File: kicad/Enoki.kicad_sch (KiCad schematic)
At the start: 14 parts, among them J1 Conn_01x08_Male

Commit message: add jlc fields
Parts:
- C1, C2, C3, C4, C5, C6: JLC (none) -> C377773
- DS1: JLC (none) -> C262569
- R1, R2, R3: JLC (none) -> C25804
- R4: value 390K -> 330K; JLC (none) -> C23137
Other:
- note added: "https://www.buydisplay.com/white-1-3-inch-oled-i2c-arduino-ssd1306-display-module-connector-fpc"
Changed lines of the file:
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@@
     (stroke (width 0) (type default))
   )
+  (text "https://www.buydisplay.com/white-1-3-inch-oled-i2c-arduino-ssd1306-display-module-connector-fpc"
+    (at 63.5 170.18 0)
+    (effects (font (size 1.27 1.27)) (justify left bottom))
+  )
   (text "https://jlcpcb.com/partdetail/Jushuo-AFC07_S30FCA00/C262569"
-    (at 100.33 162.56 0)
-    (effects (font (size 1.27 1.27)) (justify left bottom))
-  )
-  (text "Connector parts:" (at 100.33 160.02 0)
+    (at 63.5 165.1 0)
+    (effects (font (size 1.27 1.27)) (justify left bottom))
+  )
+  (text "Connector parts:" (at 63.5 162.56 0)
     (effects (font (size 1.27 1.27)) (justify left bottom))
   )
@@
       (effects (font (size 1.27 1.27)) hide)
     )
+    (property "JLC" "C25804" (at 119.38 119.38 0)
+      (effects (font (size 1.27 1.27)) hide)
+    )
     (pin "1")
     (pin "2")
@@
       (effects (font (size 1.27 1.27)) hide)
     )
+    (property "JLC" "C377773" (at 140.97 74.93 0)
+      (effects (font (size 1.27 1.27)) hide)
+    )
     (pin "1")
     (pin "2")
@@
       (effects (font (size 1.27 1.27)) hide)
     )
+    (property "JLC" "C25804" (at 119.38 87.63 0)
+      (effects (font (size 1.27 1.27)) hide)
+    )
     (pin "1")
     (pin "2")
@@
       (effects (font (size 1.27 1.27)) hide)
     )
+    (property "JLC" "C377773" (at 137.16 80.01 0)
+      (effects (font (size 1.27 1.27)) hide)
+    )
     (pin "1")
     (pin "2")
@@
       (effects (font (size 1.27 1.27)) hide)
     )
+    (property "JLC" "C377773" (at 140.97 146.05 0)
+      (effects (font (size 1.27 1.27)) hide)
+    )
     (pin "1")
     (pin "2")
@@
       (effects (font (size 1.27 1.27)) hide)
     )
+    (property "JLC" "C377773" (at 154.94 53.34 0)
+      (effects (font (size 1.27 1.27)) hide)
+    )
     (pin "1")
     (pin "2")
@@
     )
     (property "Datasheet" "https://www.vishay.com/docs/37902/oled128o064dbpp3n00000.pdf" (at 157.48 87.63 0)
+      (effects (font (size 1.27 1.27)) hide)
+    )
+    (property "JLC" "C262569" (at 157.48 107.95 0)
       (effects (font (size 1.27 1.27)) hide)
     )
@@
       (effects (font (size 1.27 1.27)))
     )
-    (property "Value" "390K" (at 125.73 147.32 0)
+    (property "Value" "330K" (at 125.73 147.32 0)
       (effects (font (size 1.27 1.27)))
     )
@@
     )
     (property "Datasheet" "~" (at 130.81 146.05 0)
+      (effects (font (size 1.27 1.27)) hide)
+    )
+    (property "JLC" "C23137" (at 130.81 146.05 0)
       (effects (font (size 1.27 1.27)) hide)
     )
@@
       (effects (font (size 1.27 1.27)) hide)
     )
+    (property "JLC" "C25804" (at 119.38 109.22 0)
+      (effects (font (size 1.27 1.27)) hide)
+    )
     (pin "1")
     (pin "2")
@@
       (effects (font (size 1.27 1.27)) hide)
     )
+    (property "JLC" "C377773" (at 160.02 63.5 0)
+      (effects (font (size 1.27 1.27)) hide)
+    )
     (pin "1")
     (pin "2")
@@
       (effects (font (size 1.27 1.27)) hide)
     )
+    (property "JLC" "C377773" (at 157.48 58.42 0)
+      (effects (font (size 1.27 1.27)) hide)
+    )

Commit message: kicad save
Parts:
- DS1: footprint Display:OLED-128O064D -> allen-synthesis:AFC07-S30FCA-00 FPC Connector 30 Pin
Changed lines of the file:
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@@
       (effects (font (size 1.27 1.27)) (justify left))
     )
-    (property "Footprint" "Display:OLED-128O064D" (at 157.48 107.95 0)
+    (property "Footprint" "allen-synthesis:AFC07-S30FCA-00 FPC Connector 30 Pin" (at 157.48 107.95 0)
       (effects (font (size 1.27 1.27)) hide)
     )

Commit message: save
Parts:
- DS1: footprint allen-synthesis:AFC07-S30FCA-00 FPC Connector 30 Pin -> allen-synthesis:KH-FPC0.5-H2.0SMT-30P-QCH FPC Connector 30 pin; JLC C262569 -> C3250002
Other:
- note added: "https://jlcpcb.com/partdetail/3812911-KH_FPC0_5_H2_0SMT_30PQCHF/C3250002"
- note removed: "https://jlcpcb.com/partdetail/Jushuo-AFC07_S30FCA00/C262569"
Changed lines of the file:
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@@
     (effects (font (size 1.27 1.27)) (justify left bottom))
   )
-  (text "https://jlcpcb.com/partdetail/Jushuo-AFC07_S30FCA00/C262569"
+  (text "https://jlcpcb.com/partdetail/3812911-KH_FPC0_5_H2_0SMT_30PQCHF/C3250002"
     (at 63.5 165.1 0)
     (effects (font (size 1.27 1.27)) (justify left bottom))
@@
       (effects (font (size 1.27 1.27)) (justify left))
     )
-    (property "Footprint" "allen-synthesis:AFC07-S30FCA-00 FPC Connector 30 Pin" (at 157.48 107.95 0)
+    (property "Footprint" "allen-synthesis:KH-FPC0.5-H2.0SMT-30P-QCH FPC Connector 30 pin" (at 157.48 107.95 0)
       (effects (font (size 1.27 1.27)) hide)
     )
@@
       (effects (font (size 1.27 1.27)) hide)
     )
-    (property "JLC" "C262569" (at 157.48 107.95 0)
-      (effects (font (size 1.27 1.27)) hide)
-    )
+    (property "JLC" "C3250002" (at 157.48 107.95 0)
+      (effects (font (size 1.27 1.27)) hide)
+    )

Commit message: save
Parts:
- added J2, J3: Conn_01x02_Pin, Connector_PinHeader_2.54mm:PinHeader_1x02_P2.54mm_Vertical_SMD_Pin1Right, symbol Connector:Conn_01x02_Pin
- J1: JLC (none) -> C5160791
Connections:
- no-connect marks 8 -> 12
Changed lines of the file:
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@@
   (no_connect (at 144.78 105.41))
   (no_connect (at 144.78 107.95))
+  (no_connect (at 77.47 127))
+  (no_connect (at 77.47 129.54))
+  (no_connect (at 77.47 114.3))
+  (no_connect (at 77.47 116.84))
   (no_connect (at 77.47 99.06))
   (wire (pts (xy 160.02 59.69) (xy 160.02 49.53))
@@
         (path "/e63e39d7-6ac0-4ffd-8aa3-1841a4541b55"
           (reference "R1") (unit 1)
+        )
+      )
+    )
+  )
+  (symbol (lib_id "Connector:Conn_01x02_Pin") (at 72.39 114.3 0) (unit 1)
+    (in_bom yes) (on_board yes) (dnp no) (fields_autoplaced)
+    (property "Reference" "J2" (at 73.025 109.22 0)
+      (effects (font (size 1.27 1.27)))
+    )
+    (property "Value" "Conn_01x02_Pin" (at 73.025 111.76 0)
+      (effects (font (size 1.27 1.27)))
+    )
+    (property "Footprint" "Connector_PinHeader_2.54mm:PinHeader_1x02_P2.54mm_Vertical_SMD_Pin1Right" (at 72.39 114.3 0)
+      (effects (font (size 1.27 1.27)) hide)
+    )
+    (property "Datasheet" "~" (at 72.39 114.3 0)
+      (effects (font (size 1.27 1.27)) hide)
+    )
+    (property "JLC" "C5160785" (at 72.39 114.3 0)
+      (effects (font (size 1.27 1.27)) hide)
+    )
+    (pin "2")
+    (pin "1")
+    (instances
+      (project "Enoki"
+        (path "/e63e39d7-6ac0-4ffd-8aa3-1841a4541b55"
+          (reference "J2") (unit 1)
         )
       )
@@
       (effects (font (size 1.27 1.27)) hide)
     )
+    (property "JLC" "C5160791" (at 72.39 88.9 0)
+      (effects (font (size 1.27 1.27)) hide)
+    )
     (pin "1")
     (pin "2")
@@
         )
       )
+    )
+  )
+  (symbol (lib_id "Connector:Conn_01x02_Pin") (at 72.39 127 0) (unit 1)
+    (in_bom yes) (on_board yes) (dnp no) (fields_autoplaced)
+    (property "Reference" "J3" (at 73.025 121.92 0)
+      (effects (font (size 1.27 1.27)))
+    )
+    (property "Value" "Conn_01x02_Pin" (at 73.025 124.46 0)
+      (effects (font (size 1.27 1.27)))
+    )
+    (property "Footprint" "Connector_PinHeader_2.54mm:PinHeader_1x02_P2.54mm_Vertical_SMD_Pin1Right" (at 72.39 127 0)
+      (effects (font (size 1.27 1.27)) hide)
+    )
+    (property "Datasheet" "~" (at 72.39 127 0)
+      (effects (font (size 1.27 1.27)) hide)
+    )
+    (property "JLC" "C5160785" (at 72.39 127 0)
+      (effects (font (size 1.27 1.27)) hide)
+    )
+    (pin "2")
+    (pin "1")
+    (instances
+      (project "Enoki"
+        (path "/e63e39d7-6ac0-4ffd-8aa3-1841a4541b55"
+          (reference "J3") (unit 1)
+        )
+      )

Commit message: save
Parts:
- JP1, JP2: footprint Jumper:SolderJumper-2_P1.3mm_Open_RoundedPad1.0x1.5mm -> Jumper:SolderJumper-2_P1.3mm_Bridged_RoundedPad1.0x1.5mm
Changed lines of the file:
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@@
       (effects (font (size 1.27 1.27)) (justify right))
     )
-    (property "Footprint" "Jumper:SolderJumper-2_P1.3mm_Open_RoundedPad1.0x1.5mm" (at 119.38 78.74 0)
+    (property "Footprint" "Jumper:SolderJumper-2_P1.3mm_Bridged_RoundedPad1.0x1.5mm" (at 119.38 78.74 0)
       (effects (font (size 1.27 1.27)) hide)
     )
@@
       (effects (font (size 1.27 1.27)) hide)
     )
-    (pin "2")
-    (pin "1")
+    (pin "1")
+    (pin "2")
     (instances
       (project "Enoki"
@@
       (effects (font (size 1.27 1.27)))
     )
-    (property "Footprint" "Jumper:SolderJumper-2_P1.3mm_Open_RoundedPad1.0x1.5mm" (at 137.16 118.11 0)
+    (property "Footprint" "Jumper:SolderJumper-2_P1.3mm_Bridged_RoundedPad1.0x1.5mm" (at 137.16 118.11 0)
       (effects (font (size 1.27 1.27)) hide)
     )
@@
       (effects (font (size 1.27 1.27)) hide)
     )
-    (pin "2")
-    (pin "1")
-    (instances
-      (project "Enoki"
+    (pin "1")
+    (pin "2")
+    (instances
+      (project "Enoki"

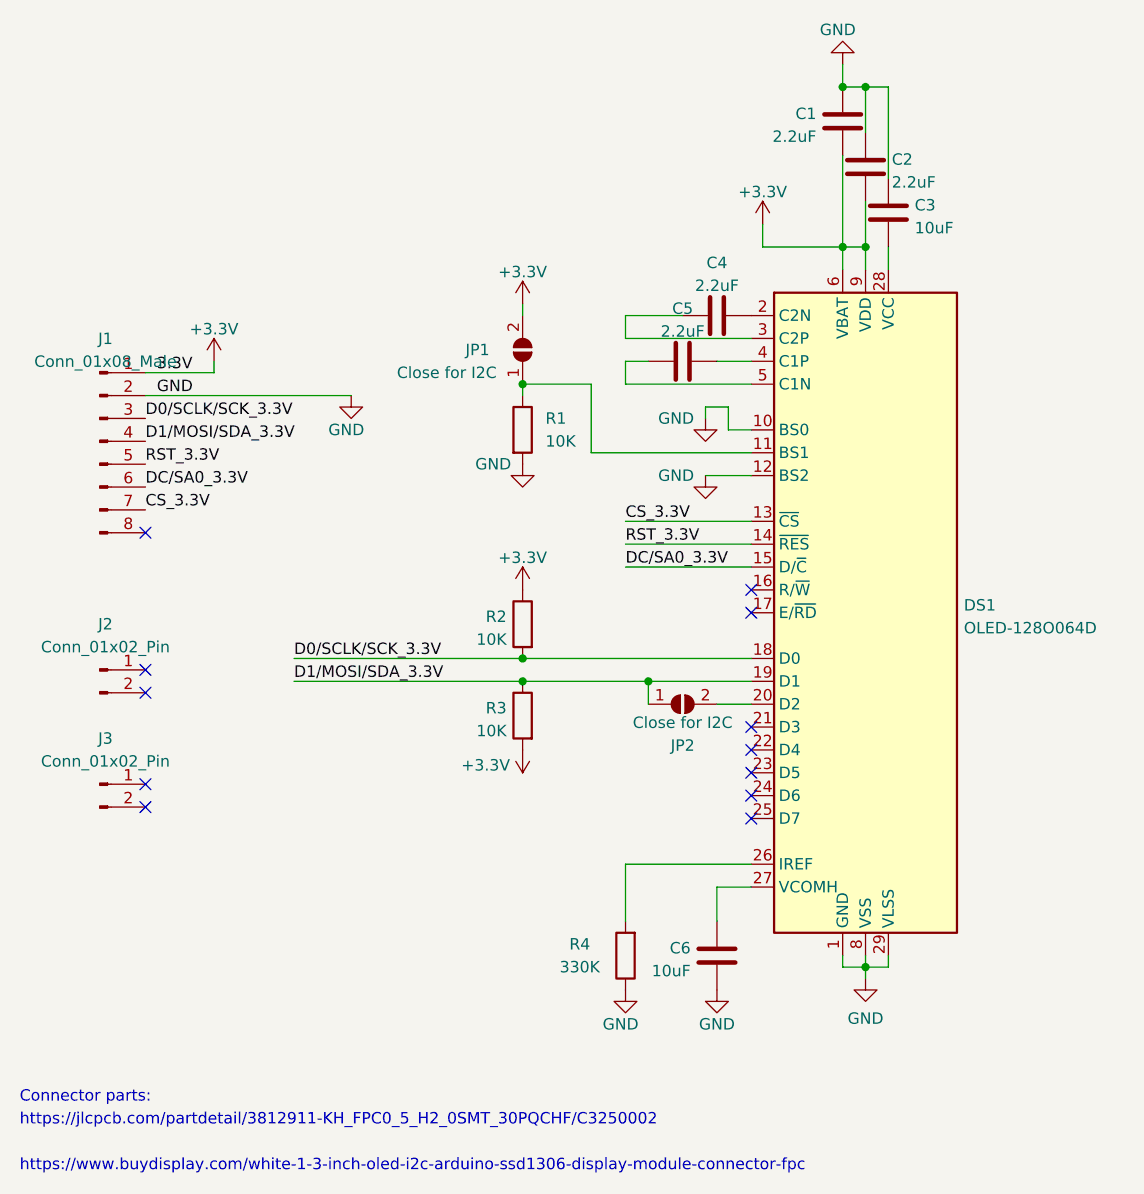
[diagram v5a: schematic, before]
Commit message: update pcb
I2C jumpers are now closed by default
RC circuit added to RST pin to remove need for manual triggering by MCU on power up
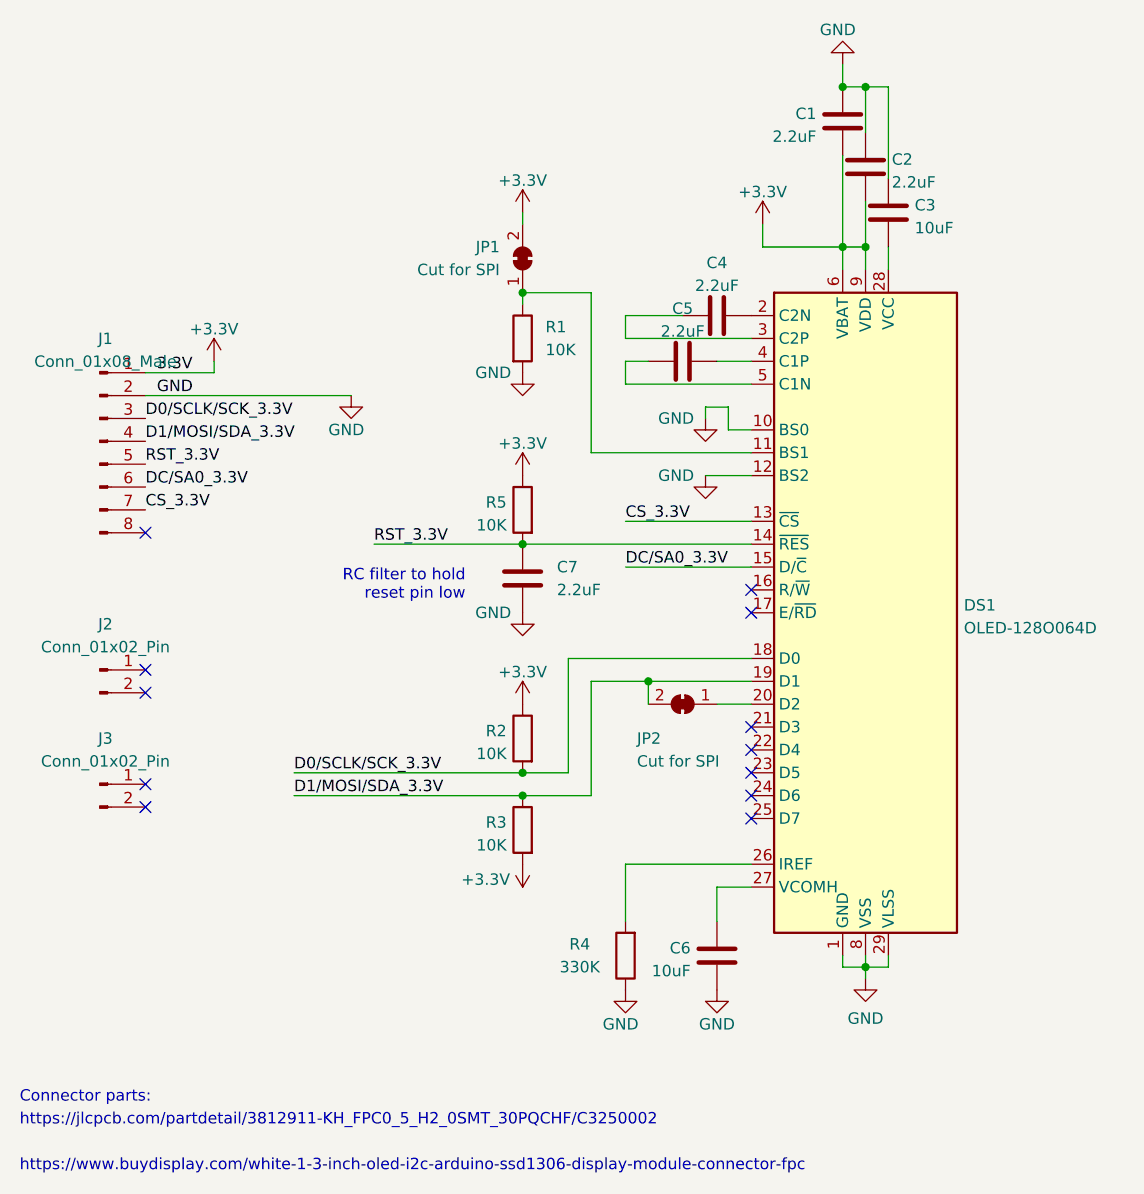
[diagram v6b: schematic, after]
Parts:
- removed JP1, JP2: Close for I2C, Jumper:SolderJumper-2_P1.3mm_Bridged_RoundedPad1.0x1.5mm, symbol Jumper:SolderJumper_2_Open
- added C7: 2.2uF, Capacitor_SMD:C_0805_2012Metric, symbol Device:C
- added JP1, JP2: Cut for SPI, Jumper:SolderJumper-2_P1.3mm_Bridged_RoundedPad1.0x1.5mm, symbol Jumper:SolderJumper_2_Bridged
- added R5: 10K, Resistor_SMD:R_0603_1608Metric, symbol Device:R
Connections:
- net +3V3: now also JP1.2 (B), R5.1
- net D1/MOSI/SDA_3.3V: now also JP2.2 (B)
- net GND: now also C7.1
- net RST_3.3V: now also C7.2, R5.2
- net at DS1.11 (BS1), R1.1: now also JP1.1 (A)
- net at DS1.20 (D2): now also JP2.1 (A)
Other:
- note added: "RC filter to hold reset pin low"
- moved on the sheet: R1, R2, R3
